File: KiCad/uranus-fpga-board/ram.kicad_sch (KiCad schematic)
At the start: 24 parts

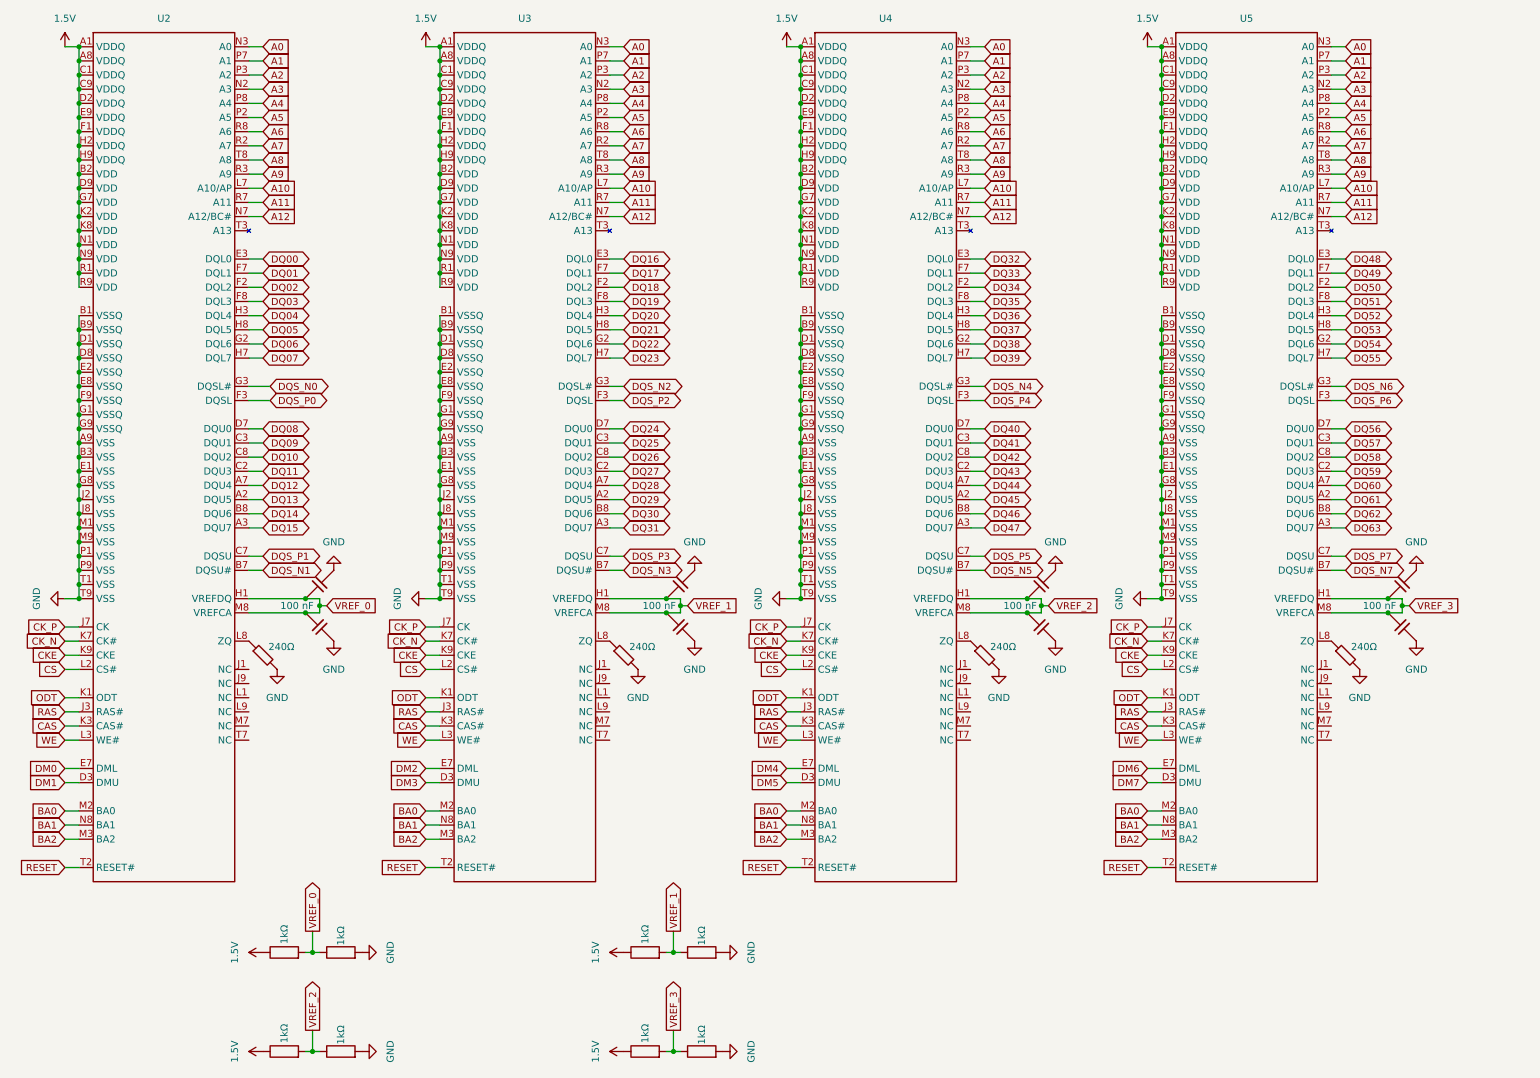
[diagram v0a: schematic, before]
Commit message: updated journal entries and BOM
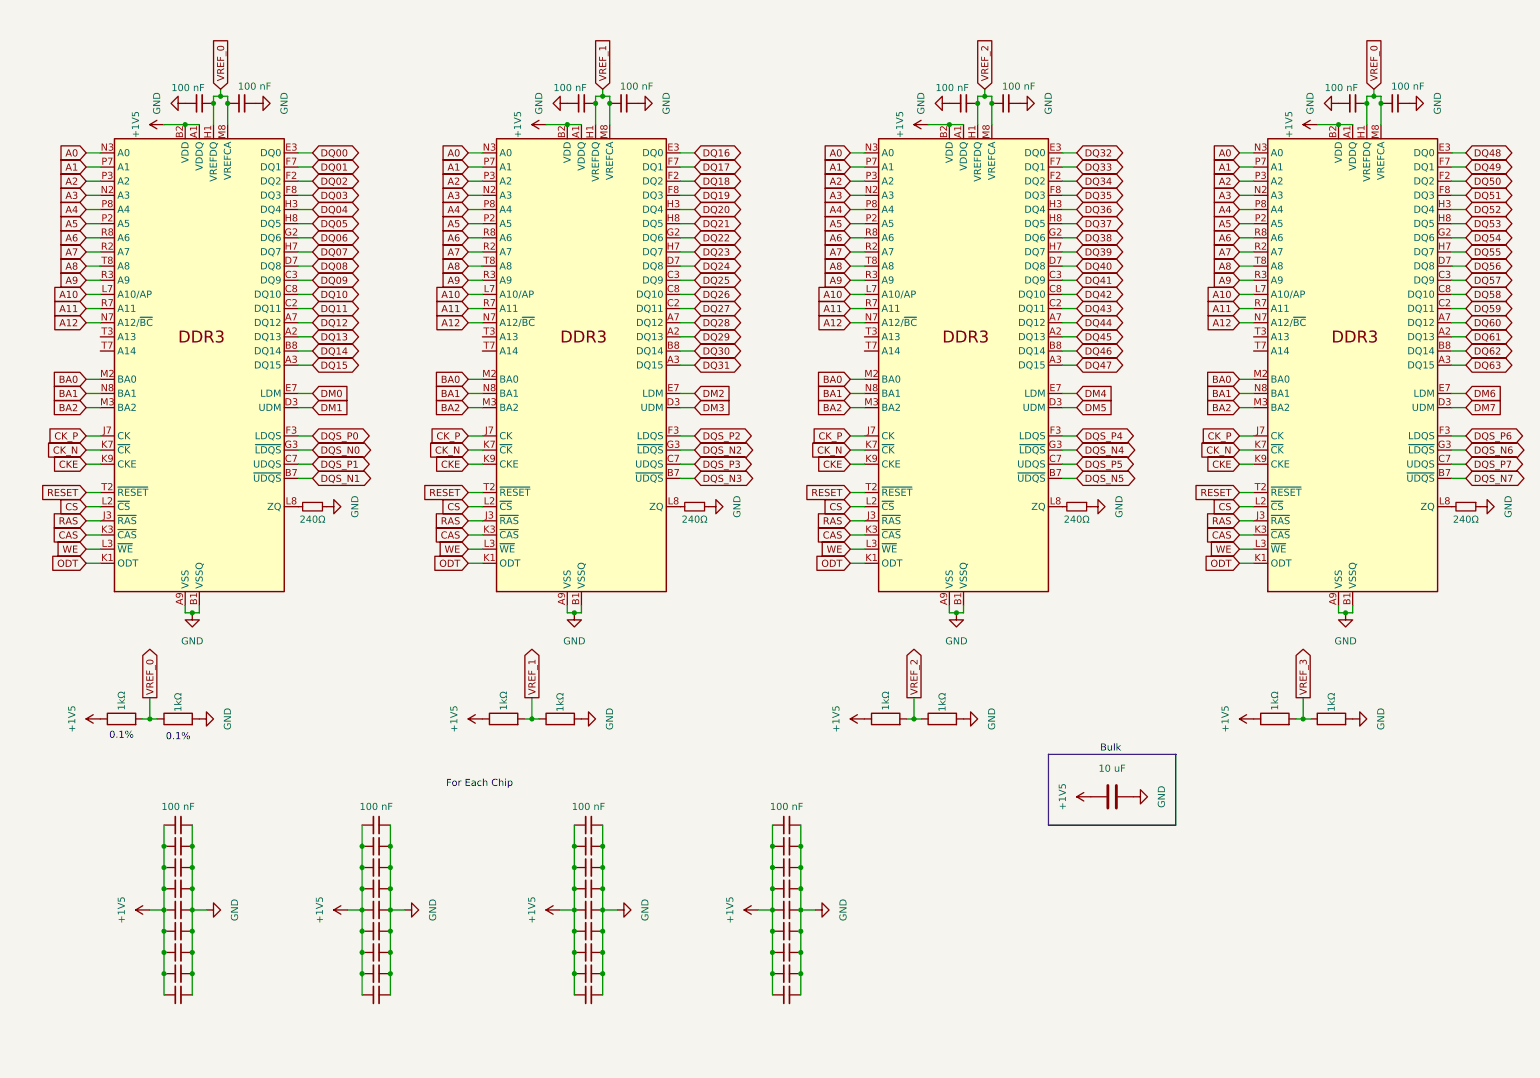
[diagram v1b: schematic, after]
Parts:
- removed 240Ω (x4): R_45deg, Package_DIP:DIP-8_W7.62mm, symbol Device:R_45deg
- removed C1, C3, C5, C7: C_45deg, symbol Device:C_45deg
- removed C2, C4, C6, C8: 100 nF, symbol Device:C_45deg
- removed U2, U3, U4, U5: (no value), W632GU6NB-11sym:, symbol W632GU6NB-11sym:W632GU6NB-11
- added C1, C18, C2, C27, C3, C36, C4, C5, C6, C7, C8, C9: 100 nF, symbol Device:C_Small
- added C10, C11, C12, C13, C14, C15, C16, C17, C19, C20, C21, C22, C23, C24, C25, C26, C28, C29, C30, C31, C32, C33, C34, C35, C37, C38, C39, C40, C41, C42, C43, C44: C_Small, symbol Device:C_Small
- added C45: 10 uF, symbol Device:C
- added R10, R11, R12, R9: 240Ω, Package_DIP:DIP-8_W7.62mm, symbol Device:R_Small
- added U6, U7, U8, U9: AS4C256M16D3, Package_BGA:FBGA-96_8x13mm_Layout9x16_P0.8mm, symbol Memory_RAM:AS4C256M16D3
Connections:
- net A0: now also U6.N3 (A0), U7.N3 (A0), U8.N3 (A0), U9.N3 (A0)
- net A1: now also U6.P7 (A1), U7.P7 (A1), U8.P7 (A1), U9.P7 (A1)
- net A10: now also U6.L7 (A10/AP), U7.L7 (A10/AP), U8.L7 (A10/AP), U9.L7 (A10/AP)
- net A11: now also U6.R7 (A11), U7.R7 (A11), U8.R7 (A11), U9.R7 (A11)
- net A12: now also U6.N7 (A12/~{BC}), U7.N7 (A12/~{BC}), U8.N7 (A12/~{BC}), U9.N7 (A12/~{BC})
- net A2: now also U6.P3 (A2), U7.P3 (A2), U8.P3 (A2), U9.P3 (A2)
- net A3: now also U6.N2 (A3), U7.N2 (A3), U8.N2 (A3), U9.N2 (A3)
- net A4: now also U6.P8 (A4), U7.P8 (A4), U8.P8 (A4), U9.P8 (A4)
- net A5: now also U6.P2 (A5), U7.P2 (A5), U8.P2 (A5), U9.P2 (A5)
- net A6: now also U6.R8 (A6), U7.R8 (A6), U8.R8 (A6), U9.R8 (A6)
- net A7: now also U6.R2 (A7), U7.R2 (A7), U8.R2 (A7), U9.R2 (A7)
- net A8: now also U6.T8 (A8), U7.T8 (A8), U8.T8 (A8), U9.T8 (A8)
- net A9: now also U6.R3 (A9), U7.R3 (A9), U8.R3 (A9), U9.R3 (A9)
- net BA0: now also U6.M2 (BA0), U7.M2 (BA0), U8.M2 (BA0), U9.M2 (BA0)
- net BA1: now also U6.N8 (BA1), U7.N8 (BA1), U8.N8 (BA1), U9.N8 (BA1)
- net BA2: now also U6.M3 (BA2), U7.M3 (BA2), U8.M3 (BA2), U9.M3 (BA2)
- net CAS: now also U6.K3 (~{CAS}), U7.K3 (~{CAS}), U8.K3 (~{CAS}), U9.K3 (~{CAS})
- net CKE: now also U6.K9 (CKE), U7.K9 (CKE), U8.K9 (CKE), U9.K9 (CKE)
- net CK_N: now also U6.K7 (~{CK}), U7.K7 (~{CK}), U8.K7 (~{CK}), U9.K7 (~{CK})
- net CK_P: now also U6.J7 (CK), U7.J7 (CK), U8.J7 (CK), U9.J7 (CK)
- net CS: now also U6.L2 (~{CS}), U7.L2 (~{CS}), U8.L2 (~{CS}), U9.L2 (~{CS})
- net DM0: now also U6.E7 (LDM)
- net DM1: now also U6.D3 (UDM)
- net DM2: now also U8.E7 (LDM)
- net DM3: now also U8.D3 (UDM)
- net DM4: now also U9.E7 (LDM)
- net DM5: now also U9.D3 (UDM)
- net DM6: now also U7.E7 (LDM)
- net DM7: now also U7.D3 (UDM)
- net DQ00: now also U6.E3 (DQ0)
- net DQ01: now also U6.F7 (DQ1)
- net DQ02: now also U6.F2 (DQ2)
- net DQ03: now also U6.F8 (DQ3)
- net DQ04: now also U6.H3 (DQ4)
- net DQ05: now also U6.H8 (DQ5)
- net DQ06: now also U6.G2 (DQ6)
- net DQ07: now also U6.H7 (DQ7)
- net DQ08: now also U6.D7 (DQ8)
- net DQ09: now also U6.C3 (DQ9)
- net DQ10: now also U6.C8 (DQ10)
- net DQ11: now also U6.C2 (DQ11)
- net DQ12: now also U6.A7 (DQ12)
- net DQ13: now also U6.A2 (DQ13)
- net DQ14: now also U6.B8 (DQ14)
- net DQ15: now also U6.A3 (DQ15)
- net DQ16: now also U8.E3 (DQ0)
- net DQ17: now also U8.F7 (DQ1)
- net DQ18: now also U8.F2 (DQ2)
- net DQ19: now also U8.F8 (DQ3)
- net DQ20: now also U8.H3 (DQ4)
- net DQ21: now also U8.H8 (DQ5)
- net DQ22: now also U8.G2 (DQ6)
- net DQ23: now also U8.H7 (DQ7)
- net DQ24: now also U8.D7 (DQ8)
- net DQ25: now also U8.C3 (DQ9)
- net DQ26: now also U8.C8 (DQ10)
- net DQ27: now also U8.C2 (DQ11)
- net DQ28: now also U8.A7 (DQ12)
- net DQ29: now also U8.A2 (DQ13)
- net DQ30: now also U8.B8 (DQ14)
- net DQ31: now also U8.A3 (DQ15)
- net DQ32: now also U9.E3 (DQ0)
- net DQ33: now also U9.F7 (DQ1)
- net DQ34: now also U9.F2 (DQ2)
- net DQ35: now also U9.F8 (DQ3)
- net DQ36: now also U9.H3 (DQ4)
- net DQ37: now also U9.H8 (DQ5)
- net DQ38: now also U9.G2 (DQ6)
- net DQ39: now also U9.H7 (DQ7)
- net DQ40: now also U9.D7 (DQ8)
- net DQ41: now also U9.C3 (DQ9)
- net DQ42: now also U9.C8 (DQ10)
- net DQ43: now also U9.C2 (DQ11)
- net DQ44: now also U9.A7 (DQ12)
- net DQ45: now also U9.A2 (DQ13)
- net DQ46: now also U9.B8 (DQ14)
- net DQ47: now also U9.A3 (DQ15)
- net DQ48: now also U7.E3 (DQ0)
- net DQ49: now also U7.F7 (DQ1)
- net DQ50: now also U7.F2 (DQ2)
- net DQ51: now also U7.F8 (DQ3)
- net DQ52: now also U7.H3 (DQ4)
- net DQ53: now also U7.H8 (DQ5)
- net DQ54: now also U7.G2 (DQ6)
- net DQ55: now also U7.H7 (DQ7)
- net DQ56: now also U7.D7 (DQ8)
- net DQ57: now also U7.C3 (DQ9)
- net DQ58: now also U7.C8 (DQ10)
- net DQ59: now also U7.C2 (DQ11)
- net DQ60: now also U7.A7 (DQ12)
- net DQ61: now also U7.A2 (DQ13)
- net DQ62: now also U7.B8 (DQ14)
- net DQ63: now also U7.A3 (DQ15)
- net DQS_N0: now also U6.G3 (~{LDQS})
- net DQS_N1: now also U6.B7 (~{UDQS})
- net DQS_N2: now also U8.G3 (~{LDQS})
- net DQS_N3: now also U8.B7 (~{UDQS})
- net DQS_N4: now also U9.G3 (~{LDQS})
- net DQS_N5: now also U9.B7 (~{UDQS})
- net DQS_N6: now also U7.G3 (~{LDQS})
- net DQS_N7: now also U7.B7 (~{UDQS})
- net DQS_P0: now also U6.F3 (LDQS)
- net DQS_P1: now also U6.C7 (UDQS)
- net DQS_P2: now also U8.F3 (LDQS)
- net DQS_P3: now also U8.C7 (UDQS)
- net DQS_P4: now also U9.F3 (LDQS)
- net DQS_P5: now also U9.C7 (UDQS)
- net DQS_P6: now also U7.F3 (LDQS)
- net DQS_P7: now also U7.C7 (UDQS)
- net GND: now also C1.1, C10.2, C11.2, C12.2, C13.2, C14.2, C15.2, C16.2, C17.2, C18.2, C19.2, C2.2, C20.2, C21.2, C22.2, C23.2, C24.2, C25.2, C26.2, C27.2, C28.2, C29.2, C3.1, C30.2, C31.2, C32.2, C33.2, C34.2, C35.2, C36.2, C37.2, C38.2, C39.2, C4.2, C40.2, C41.2, C42.2, C43.2, C44.2, C45.2, C5.1, C6.2, C7.1, C8.2, C9.2, R10.1, R11.1, R12.1, R9.1, U6.A9 (VSS), U6.B1 (VSSQ), U6.B3 (VSS), U6.B9 (VSSQ), U6.D1 (VSSQ), U6.D8 (VSSQ), U6.E1 (VSS), U6.E2 (VSSQ), U6.E8 (VSSQ), U6.F9 (VSSQ), U6.G1 (VSSQ), U6.G8 (VSS), U6.G9 (VSSQ), U6.J2 (VSS), U6.J8 (VSS), U6.M1 (VSS), U6.M9 (VSS), U6.P1 (VSS), U6.P9 (VSS), U6.T1 (VSS), U6.T9 (VSS), U7.A9 (VSS), U7.B1 (VSSQ), U7.B3 (VSS), U7.B9 (VSSQ), U7.D1 (VSSQ), U7.D8 (VSSQ), U7.E1 (VSS), U7.E2 (VSSQ), U7.E8 (VSSQ), U7.F9 (VSSQ), U7.G1 (VSSQ), U7.G8 (VSS), U7.G9 (VSSQ), U7.J2 (VSS), U7.J8 (VSS), U7.M1 (VSS), U7.M9 (VSS), U7.P1 (VSS), U7.P9 (VSS), U7.T1 (VSS), U7.T9 (VSS), U8.A9 (VSS), U8.B1 (VSSQ), U8.B3 (VSS), U8.B9 (VSSQ), U8.D1 (VSSQ), U8.D8 (VSSQ), U8.E1 (VSS), U8.E2 (VSSQ), U8.E8 (VSSQ), U8.F9 (VSSQ), U8.G1 (VSSQ), U8.G8 (VSS), U8.G9 (VSSQ), U8.J2 (VSS), U8.J8 (VSS), U8.M1 (VSS), U8.M9 (VSS), U8.P1 (VSS), U8.P9 (VSS), U8.T1 (VSS), U8.T9 (VSS), U9.A9 (VSS), U9.B1 (VSSQ), U9.B3 (VSS), U9.B9 (VSSQ), U9.D1 (VSSQ), U9.D8 (VSSQ), U9.E1 (VSS), U9.E2 (VSSQ), U9.E8 (VSSQ), U9.F9 (VSSQ), U9.G1 (VSSQ), U9.G8 (VSS), U9.G9 (VSSQ), U9.J2 (VSS), U9.J8 (VSS), U9.M1 (VSS), U9.M9 (VSS), U9.P1 (VSS), U9.P9 (VSS), U9.T1 (VSS), U9.T9 (VSS)
- net ODT: now also U6.K1 (ODT), U7.K1 (ODT), U8.K1 (ODT), U9.K1 (ODT)
- net RAS: now also U6.J3 (~{RAS}), U7.J3 (~{RAS}), U8.J3 (~{RAS}), U9.J3 (~{RAS})
- net RESET: now also U6.T2 (~{RESET}), U7.T2 (~{RESET}), U8.T2 (~{RESET}), U9.T2 (~{RESET})
- net VREF_0: now also C1.2, C2.1, C3.2, C4.1, U6.H1 (VREFDQ), U6.M8 (VREFCA), U7.H1 (VREFDQ), U7.M8 (VREFCA)
- net VREF_1: now also C5.2, C6.1, U8.H1 (VREFDQ), U8.M8 (VREFCA)
- net VREF_2: now also C7.2, C8.1, U9.H1 (VREFDQ), U9.M8 (VREFCA)
- net WE: now also U6.L3 (~{WE}), U7.L3 (~{WE}), U8.L3 (~{WE}), U9.L3 (~{WE})
- net 1.5V renamed +1V5
- net +1V5: now also C10.1, C11.1, C12.1, C13.1, C14.1, C15.1, C16.1, C17.1, C18.1, C19.1, C20.1, C21.1, C22.1, C23.1, C24.1, C25.1, C26.1, C27.1, C28.1, C29.1, C30.1, C31.1, C32.1, C33.1, C34.1, C35.1, C36.1, C37.1, C38.1, C39.1, C40.1, C41.1, C42.1, C43.1, C44.1, C45.1, C9.1, U6.A1 (VDDQ), U6.A8 (VDDQ), U6.B2 (VDD), U6.C1 (VDDQ), U6.C9 (VDDQ), U6.D2 (VDDQ), U6.D9 (VDD), U6.E9 (VDDQ), U6.F1 (VDDQ), U6.G7 (VDD), U6.H2 (VDDQ), U6.H9 (VDDQ), U6.K2 (VDD), U6.K8 (VDD), U6.N1 (VDD), U6.N9 (VDD), U6.R1 (VDD), U6.R9 (VDD), U7.A1 (VDDQ), U7.A8 (VDDQ), U7.B2 (VDD), U7.C1 (VDDQ), U7.C9 (VDDQ), U7.D2 (VDDQ), U7.D9 (VDD), U7.E9 (VDDQ), U7.F1 (VDDQ), U7.G7 (VDD), U7.H2 (VDDQ), U7.H9 (VDDQ), U7.K2 (VDD), U7.K8 (VDD), U7.N1 (VDD), U7.N9 (VDD), U7.R1 (VDD), U7.R9 (VDD), U8.A1 (VDDQ), U8.A8 (VDDQ), U8.B2 (VDD), U8.C1 (VDDQ), U8.C9 (VDDQ), U8.D2 (VDDQ), U8.D9 (VDD), U8.E9 (VDDQ), U8.F1 (VDDQ), U8.G7 (VDD), U8.H2 (VDDQ), U8.H9 (VDDQ), U8.K2 (VDD), U8.K8 (VDD), U8.N1 (VDD), U8.N9 (VDD), U8.R1 (VDD), U8.R9 (VDD), U9.A1 (VDDQ), U9.A8 (VDDQ), U9.B2 (VDD), U9.C1 (VDDQ), U9.C9 (VDDQ), U9.D2 (VDDQ), U9.D9 (VDD), U9.E9 (VDDQ), U9.F1 (VDDQ), U9.G7 (VDD), U9.H2 (VDDQ), U9.H9 (VDDQ), U9.K2 (VDD), U9.K8 (VDD), U9.N1 (VDD), U9.N9 (VDD), U9.R1 (VDD), U9.R9 (VDD)
- new net: R9.2, U6.L8 (ZQ)
- new net: R12.2, U9.L8 (ZQ)
- new net: R11.2, U8.L8 (ZQ)
- new net: R10.2, U7.L8 (ZQ)
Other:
- note added: "0.1%"
- note added: "Bulk"
- note added: "For Each Chip"
